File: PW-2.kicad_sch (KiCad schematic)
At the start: 33 parts

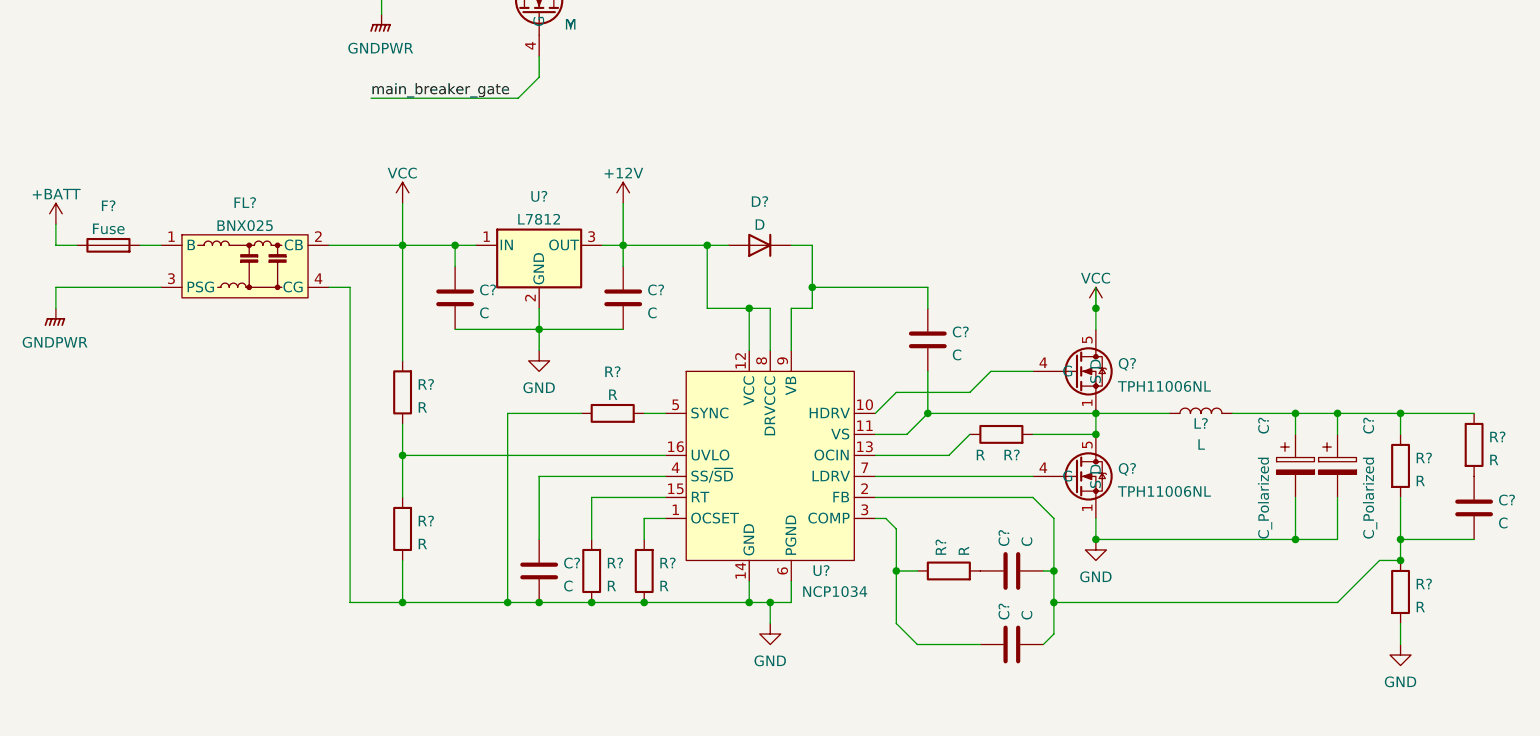
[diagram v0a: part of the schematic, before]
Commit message: separate to some sheets
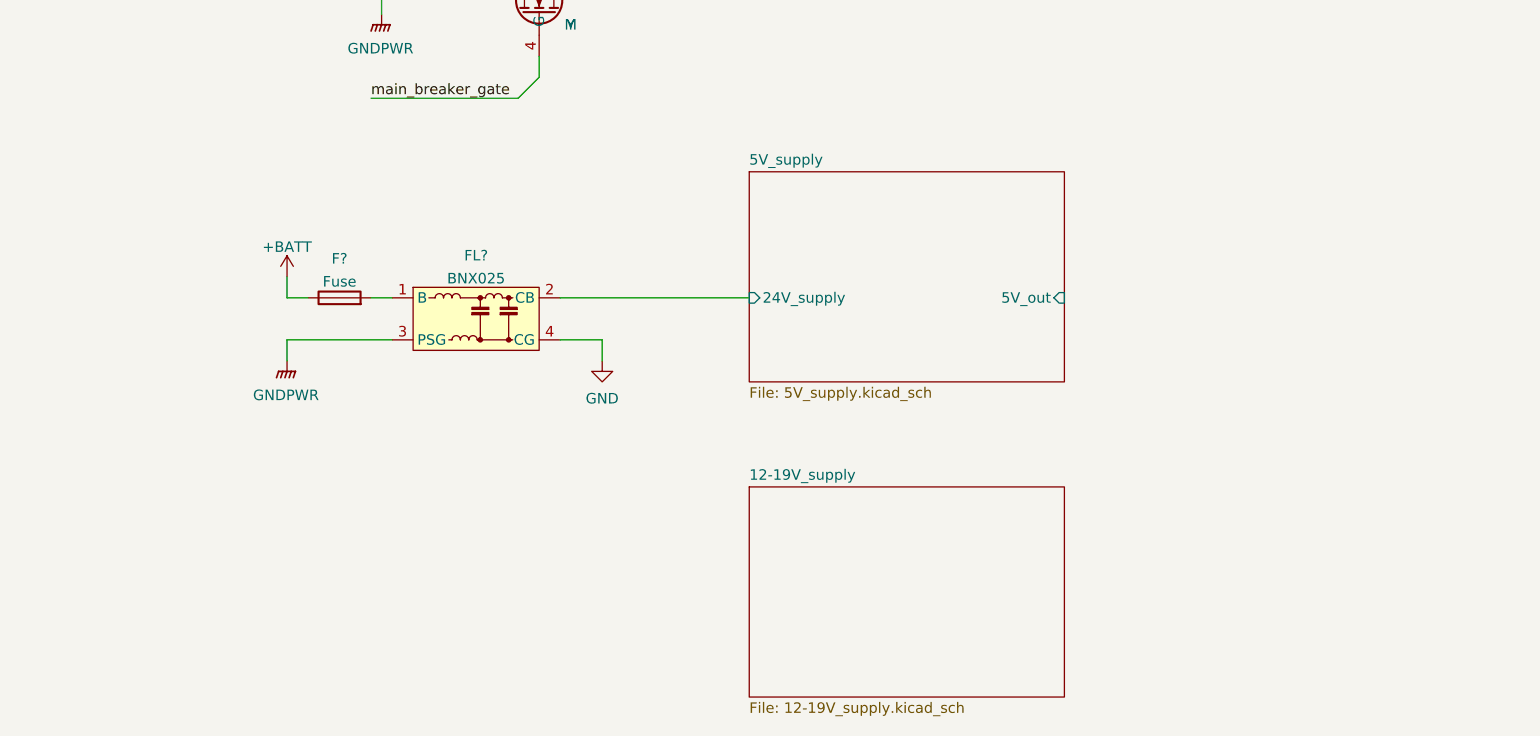
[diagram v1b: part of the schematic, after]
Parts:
- removed C? (x7): C, symbol Device:C
- removed C? (x2): C_Polarized, symbol Device:C_Polarized
- removed D?: D, symbol Device:D
- removed L?: L, symbol Device:L
- removed Q? (x2): TPH11006NL, Package_SON_additional:Toshiba_SOP_Advance, symbol Transistor_FET_additional:TPH11006NL
- removed R? (x10): R, symbol Device:R
- removed U?: NCP1034, Package_SO:SOIC-16_3.9x9.9mm_P1.27mm, symbol Regulator_Switching_additional:NCP1034
- removed U?: L7812, symbol Regulator_Linear:L7812
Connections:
- net VCC renamed 5V_supply/24V_supply
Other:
- added sheet 12-19V_supply (12-19V_supply.kicad_sch)
- added sheet 5V_supply (5V_supply.kicad_sch)
- moved on the sheet: F?, FL?

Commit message: little change
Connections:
- net 5V_supply/24V_supply renamed 12-19V_supply/24V_supply
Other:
- sheet 12-19V_supply ports: added 12-19V_out, 24V_supply; removed none
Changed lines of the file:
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@@
   (junction (at 69.85 80.01) (diameter 0) (color 0 0 0 0)
   )
+  (junction (at 106.68 116.84) (diameter 0) (color 0 0 0 0)
+  )
   (junction (at 82.55 60.96) (diameter 0) (color 0 0 0 0)
   )
@@
     (stroke (width 0) (type default) (color 0 0 0 0))
   )
+  (wire (pts (xy 106.68 116.84) (xy 114.3 116.84))
+    (stroke (width 0) (type default) (color 0 0 0 0))
+  )
   (wire (pts (xy 58.42 121.92) (xy 58.42 124.46))
     (stroke (width 0) (type default) (color 0 0 0 0))
@@
     (stroke (width 0) (type default) (color 0 0 0 0))
   )
+  (wire (pts (xy 106.68 154.94) (xy 114.3 154.94))
+    (stroke (width 0) (type default) (color 0 0 0 0))
+  )
   (wire (pts (xy 91.44 121.92) (xy 96.52 121.92))
     (stroke (width 0) (type default) (color 0 0 0 0))
   )
+  (wire (pts (xy 106.68 116.84) (xy 106.68 154.94))
+    (stroke (width 0) (type default) (color 0 0 0 0))
+  )
   (wire (pts (xy 82.55 68.58) (xy 82.55 60.96))
     (stroke (width 0) (type default) (color 0 0 0 0))
@@
     (stroke (width 0) (type default) (color 0 0 0 0))
   )
-  (wire (pts (xy 91.44 116.84) (xy 114.3 116.84))
+  (wire (pts (xy 91.44 116.84) (xy 106.68 116.84))
     (stroke (width 0) (type default) (color 0 0 0 0))
   )
@@
       (effects (font (size 1.27 1.27)) (justify left top))
     )
+    (pin "12-19V_out" input (at 152.4 154.94 0)
+      (effects (font (size 1.27 1.27)) (justify right))
+    )
+    (pin "24V_supply" input (at 114.3 154.94 180)
+      (effects (font (size 1.27 1.27)) (justify left))
+    )
   )
   (sheet_instances
@@
       (reference "#PWR?") (unit 1) (value "GND") (footprint "")
     )
+    (path "/84b8b3f7-2160-474c-a31d-5c409d471e1e/83899034-d72b-4d72-b360-2350e96bde69"
+      (reference "#PWR?") (unit 1) (value "GND") (footprint "")
+    )
     (path "/8eb5e770-d904-422f-814b-21543d34976a"
       (reference "#PWR?") (unit 1) (value "+BATT") (footprint "")
@@
       (reference "#PWR?") (unit 1) (value "GND") (footprint "")
     )
-    (path "/823bdb72-b3da-47c7-8be1-d919cd2d99f3/e14baf8b-f165-42d0-ab67-48db2ef1f110"
-      (reference "#PWR?") (unit 1) (value "VCC") (footprint "")
+    (path "/84b8b3f7-2160-474c-a31d-5c409d471e1e/dec7721f-253a-41eb-9287-d0b7bc694215"
+      (reference "#PWR?") (unit 1) (value "GND") (footprint "")
+    )
+    (path "/84b8b3f7-2160-474c-a31d-5c409d471e1e/e94dfe8b-2a89-44d2-beec-206a1417d69d"
+      (reference "#PWR?") (unit 1) (value "GND") (footprint "")
+    )
+    (path "/84b8b3f7-2160-474c-a31d-5c409d471e1e/fb3e2d6c-4b5a-4d47-a9b4-2295f98d4544"
+      (reference "#PWR?") (unit 1) (value "GND") (footprint "")
+    )
+    (path "/84b8b3f7-2160-474c-a31d-5c409d471e1e/0a2588dd-ff9e-4076-aca8-67f53d693bb4"
+      (reference "C?") (unit 1) (value "C") (footprint "")
+    )
+    (path "/84b8b3f7-2160-474c-a31d-5c409d471e1e/1204c0ac-59fa-44de-8b10-b01950f18222"
+      (reference "C?") (unit 1) (value "C") (footprint "")
     )
     (path "/823bdb72-b3da-47c7-8be1-d919cd2d99f3/1b8e1adc-7f25-4d14-bb59-2234667c7f99"
@@
       (reference "C?") (unit 1) (value "C") (footprint "")
     )
+    (path "/84b8b3f7-2160-474c-a31d-5c409d471e1e/3495c038-ec42-4aed-a10f-66c3d42af889"
+      (reference "C?") (unit 1) (value "C") (footprint "")
+    )
     (path "/823bdb72-b3da-47c7-8be1-d919cd2d99f3/592af23c-e24e-4241-b105-046834f9f8db"
       (reference "C?") (unit 1) (value "C") (footprint "")
     )
+    (path "/84b8b3f7-2160-474c-a31d-5c409d471e1e/6e69e5c9-097d-4c66-9fbb-33c4cc2a46b9"
+      (reference "C?") (unit 1) (value "C_Polarized") (footprint "")
+    )
+    (path "/84b8b3f7-2160-474c-a31d-5c409d471e1e/71de5c5c-f9d4-4846-b4ed-512bbf279aae"
+      (reference "C?") (unit 1) (value "C") (footprint "")
+    )
+    (path "/84b8b3f7-2160-474c-a31d-5c409d471e1e/7a683382-1dbf-447f-8e83-d7e70b931d63"
+      (reference "C?") (unit 1) (value "C_Polarized") (footprint "")
+    )
     (path "/823bdb72-b3da-47c7-8be1-d919cd2d99f3/7b5f0e0d-8f2b-4349-b8f9-0cad599e3694"
       (reference "C?") (unit 1) (value "C") (footprint "")
     )
+    (path "/84b8b3f7-2160-474c-a31d-5c409d471e1e/84735774-4e83-4228-a9b4-8d0334297691"
+      (reference "C?") (unit 1) (value "C") (footprint "")
+    )
+    (path "/84b8b3f7-2160-474c-a31d-5c409d471e1e/97add672-33fd-4881-a493-e1f46f53eac3"
+      (reference "C?") (unit 1) (value "C") (footprint "")
+    )
     (path "/823bdb72-b3da-47c7-8be1-d919cd2d99f3/a3ba4a17-7310-4e11-bf4f-c2894df162a5"
+      (reference "C?") (unit 1) (value "C") (footprint "")
+    )
+    (path "/84b8b3f7-2160-474c-a31d-5c409d471e1e/c19d2924-d975-404d-a72e-317851bf72a8"
       (reference "C?") (unit 1) (value "C") (footprint "")
     )
@@
       (reference "D?") (unit 1) (value "D") (footprint "")
     )
+    (path "/84b8b3f7-2160-474c-a31d-5c409d471e1e/ac3e7469-dad1-4aeb-afc7-66de12c1386f"
+      (reference "D?") (unit 1) (value "D") (footprint "")
+    )
     (path "/15042728-0ae4-4179-835c-8dc250275282"
       (reference "F?") (unit 1) (value "Fuse") (footprint "")
@@
       (reference "L?") (unit 1) (value "L") (footprint "")
     )
+    (path "/84b8b3f7-2160-474c-a31d-5c409d471e1e/27ac9651-6e7f-4ab4-9a0f-f09788d07fca"
+      (reference "L?") (unit 1) (value "L") (footprint "")
+    )
     (path "/0db8a049-a6a2-4724-ac1c-20b36cc3d210"
       (reference "Q?") (unit 1) (value "BSC025N08LS5") (footprint "Package_TO_SOT_SMD:TDSON-8-1")
     )
+    (path "/84b8b3f7-2160-474c-a31d-5c409d471e1e/129519b5-bc1e-406a-b3ff-f03ddcb3f164"
+      (reference "Q?") (unit 1) (value "TPH11006NL") (footprint "Package_SON_additional:Toshiba_SOP_Advance")
+    )
     (path "/823bdb72-b3da-47c7-8be1-d919cd2d99f3/1dd65e06-1b19-42b2-9e48-aa593ac50db3"
       (reference "Q?") (unit 1) (value "TPH11006NL") (footprint "Package_SON_additional:Toshiba_SOP_Advance")
@@
       (reference "Q?") (unit 1) (value "TPH11006NL") (footprint "Package_SON_additional:Toshiba_SOP_Advance")
     )
+    (path "/84b8b3f7-2160-474c-a31d-5c409d471e1e/dbb70a15-b598-4a56-968a-fd2790b3ef10"
+      (reference "Q?") (unit 1) (value "TPH11006NL") (footprint "Package_SON_additional:Toshiba_SOP_Advance")
+    )
     (path "/823bdb72-b3da-47c7-8be1-d919cd2d99f3/29de0295-fc98-4e91-b33d-3538007ba123"
       (reference "R?") (unit 1) (value "R") (footprint "")
     )
+    (path "/84b8b3f7-2160-474c-a31d-5c409d471e1e/323ddd7f-366b-4dd9-8d22-bc62470b5400"
+      (reference "R?") (unit 1) (value "R") (footprint "")
+    )
+    (path "/84b8b3f7-2160-474c-a31d-5c409d471e1e/33144a3b-72d8-40ac-9078-472f89108441"
+      (reference "R?") (unit 1) (value "R") (footprint "")
+    )
+    (path "/84b8b3f7-2160-474c-a31d-5c409d471e1e/3bb94b23-9013-4619-b4ff-d766a57dfc11"
+      (reference "R?") (unit 1) (value "R") (footprint "")
+    )
     (path "/823bdb72-b3da-47c7-8be1-d919cd2d99f3/4d911753-8c1e-4602-894e-048d993310df"
       (reference "R?") (unit 1) (value "R") (footprint "")
     )
+    (path "/84b8b3f7-2160-474c-a31d-5c409d471e1e/5a4580a8-da55-4ce3-bbbe-b33e7f00faa6"
+      (reference "R?") (unit 1) (value "R") (footprint "")
+    )
+    (path "/84b8b3f7-2160-474c-a31d-5c409d471e1e/78a9b55b-caff-4420-a6ae-19a7131d97be"
+      (reference "R?") (unit 1) (value "R") (footprint "")
+    )
     (path "/823bdb72-b3da-47c7-8be1-d919cd2d99f3/81b97e70-46f3-4336-aebf-837d4cb8d978"
       (reference "R?") (unit 1) (value "R") (footprint "")
@@
       (reference "R?") (unit 1) (value "R") (footprint "")
     )
+    (path "/84b8b3f7-2160-474c-a31d-5c409d471e1e/c67835f5-9fb5-486a-ab9c-a3a0a5f39d1e"
+      (reference "R?") (unit 1) (value "R") (footprint "")
+    )
     (path "/823bdb72-b3da-47c7-8be1-d919cd2d99f3/d8fc968d-0334-4506-9468-5085bda493cb"
       (reference "R?") (unit 1) (value "R") (footprint "")
@@
       (reference "R?") (unit 1) (value "R") (footprint "")
     )
+    (path "/84b8b3f7-2160-474c-a31d-5c409d471e1e/e165e83c-6f01-4850-ac2e-250d8cb59303"
+      (reference "R?") (unit 1) (value "R") (footprint "")
+    )
+    (path "/84b8b3f7-2160-474c-a31d-5c409d471e1e/ea8a827f-ae0c-4cf1-8927-35f036a4c0c6"
+      (reference "R?") (unit 1) (value "R") (footprint "")
+    )
     (path "/823bdb72-b3da-47c7-8be1-d919cd2d99f3/edd60eb5-f9d0-4f79-b305-7623d2945a46"
+      (reference "R?") (unit 1) (value "R") (footprint "")
+    )
+    (path "/84b8b3f7-2160-474c-a31d-5c409d471e1e/f1b0a714-9b6c-48c5-8716-22beeb389c64"
+      (reference "R?") (unit 1) (value "R") (footprint "")
+    )
+    (path "/84b8b3f7-2160-474c-a31d-5c409d471e1e/fa309369-28f1-4e35-9688-c2cc9b3d2b38"
       (reference "R?") (unit 1) (value "R") (footprint "")
     )
@@
       (reference "U?") (unit 1) (value "NCP1034") (footprint "Package_SO:SOIC-16_3.9x9.9mm_P1.27mm")
     )
+    (path "/84b8b3f7-2160-474c-a31d-5c409d471e1e/ddbf5ec5-6bcd-435d-aef5-27df202a0f49"
+      (reference "U?") (unit 1) (value "L7812") (footprint "")
+    )
+    (path "/84b8b3f7-2160-474c-a31d-5c409d471e1e/e82879b1-7983-4342-85c0-816b129eca36"
+      (reference "U?") (unit 1) (value "NCP1034") (footprint "Package_SO:SOIC-16_3.9x9.9mm_P1.27mm")
+    )

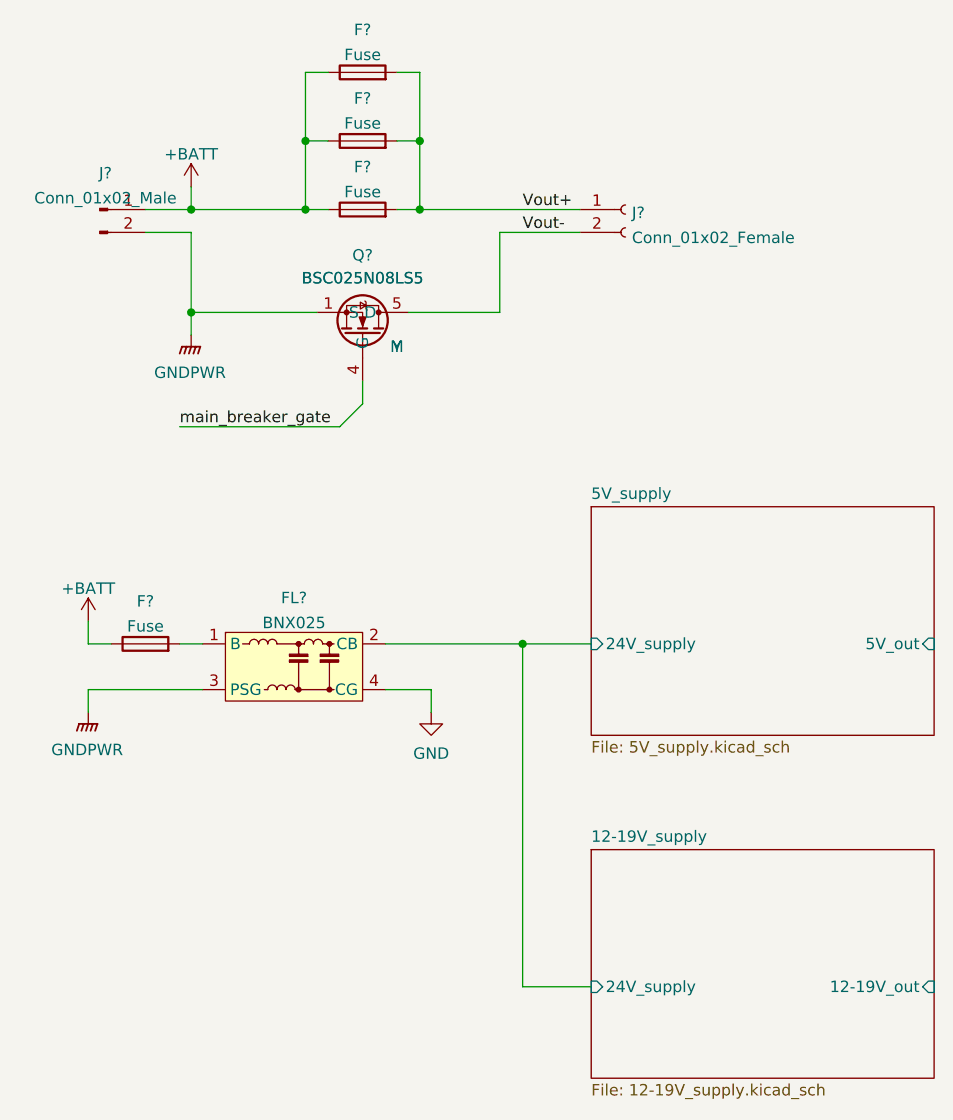
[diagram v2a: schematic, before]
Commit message: DC-DC pram setted
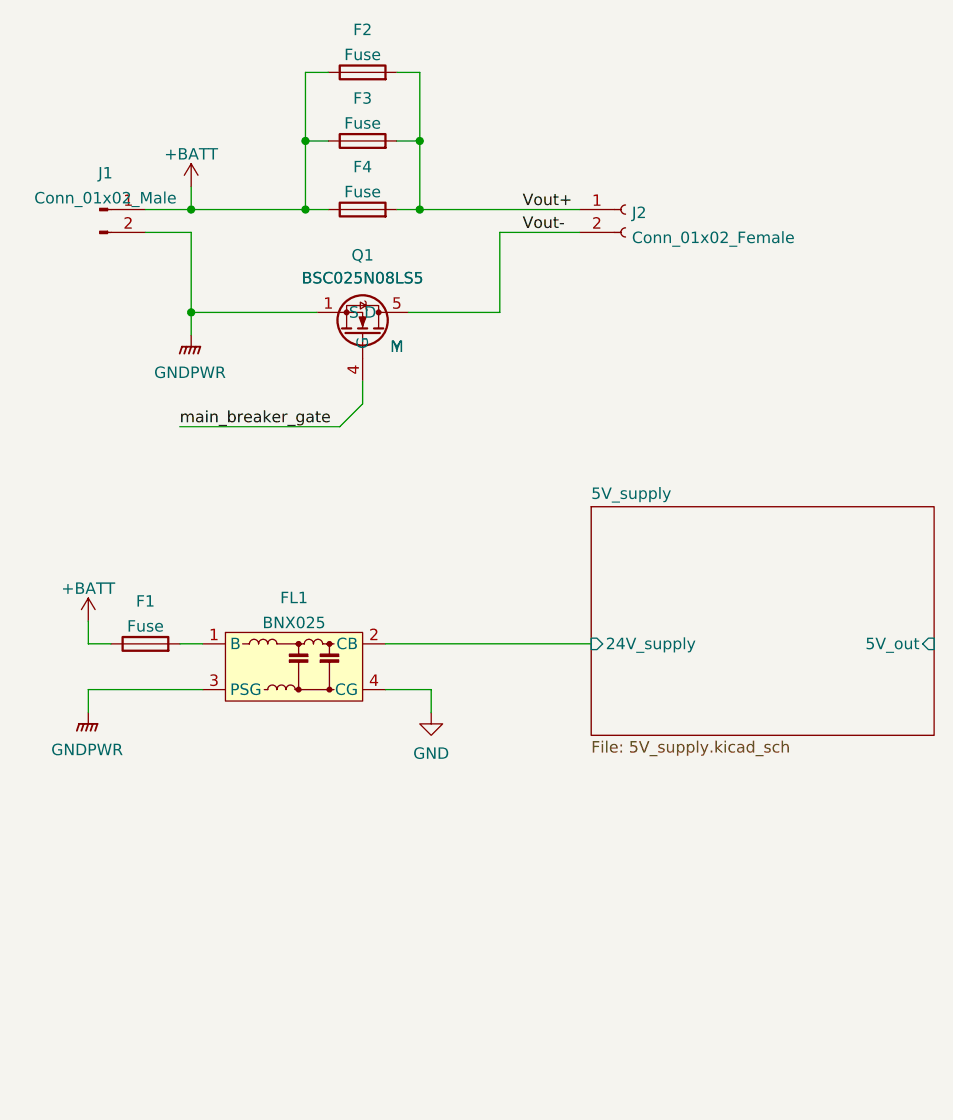
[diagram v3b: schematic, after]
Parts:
- gave numbers to parts that had none: 8
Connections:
- net 12-19V_supply/24V_supply renamed 5V_supply/24V_supply
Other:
- removed sheet 12-19V_supply

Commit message: connectors
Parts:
- added J? (x2): USB_A_Stacked, Connector_USB:USB_A_Wuerth_61400826021_Horizontal_Stacked, symbol Connector:USB_A_Stacked
- FL1: value BNX025 -> BNX022; footprint Filter:Filter_Murata_BNX025 -> Filter:Filter_Murata_BNX025_ThermalVias
- J1: footprint (none) -> Connector_T_connector:T_connecter_male_horizontal
- J2: footprint (none) -> Connector_T_connector:T_connecter_female_horizontal
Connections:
- net GND: now also J?.4 (GND1), J?.4 (GND1), J?.8 (GND2), J?.8 (GND2), J?.9 (Shield), J?.9 (Shield)
- new net: J?.2 (D1-), J?.3 (D1+) (x2)
- new net: J?.6 (D2-), J?.7 (D2+) (x2)
- new net +5V: J?.1 (VBUS1), J?.1 (VBUS1), J?.5 (VBUS2), J?.5 (VBUS2)
